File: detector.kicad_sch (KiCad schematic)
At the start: 16 parts, among them Q3 KT315, U1 74HC08, U5 LM339

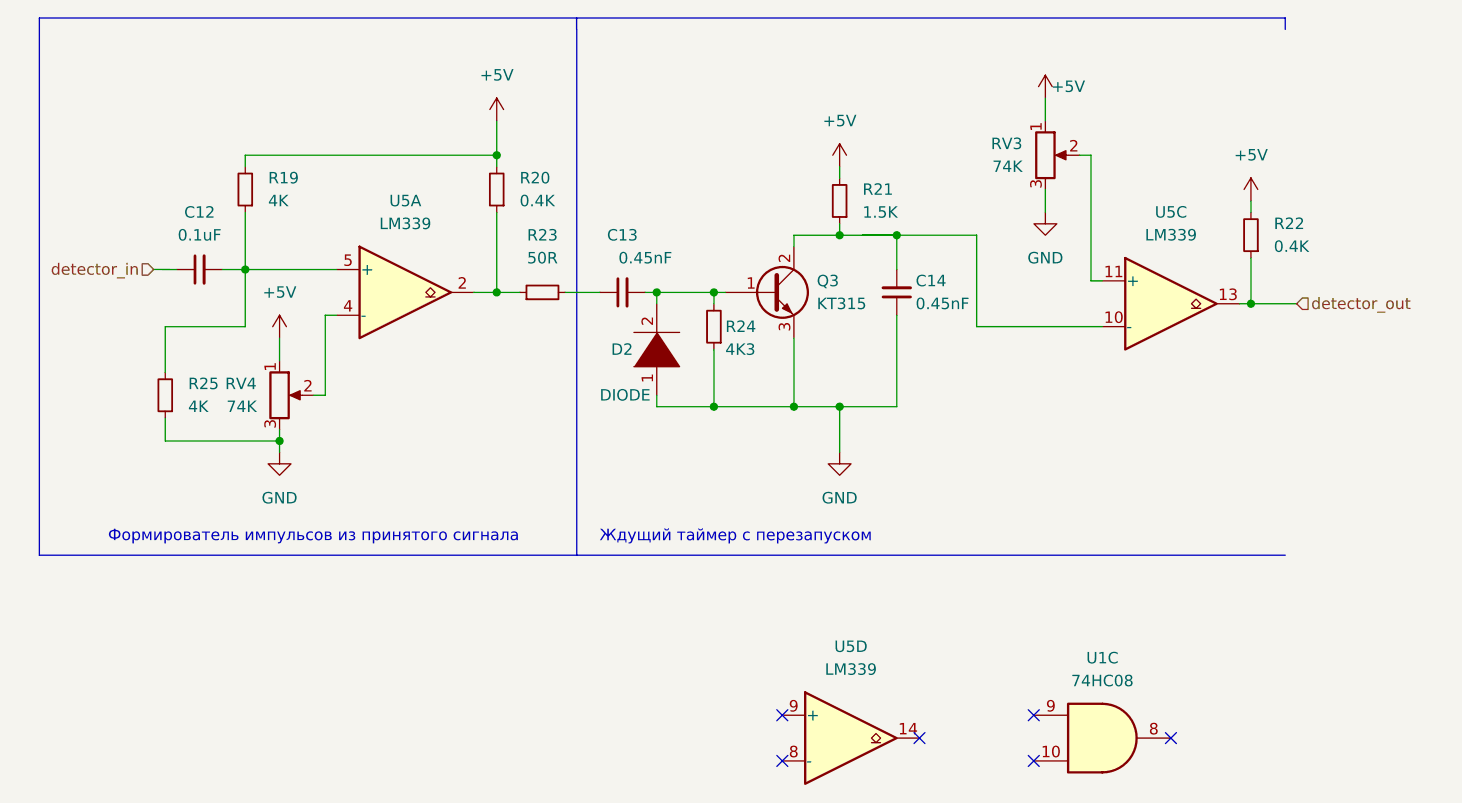
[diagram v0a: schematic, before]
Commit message: test points and some silk added
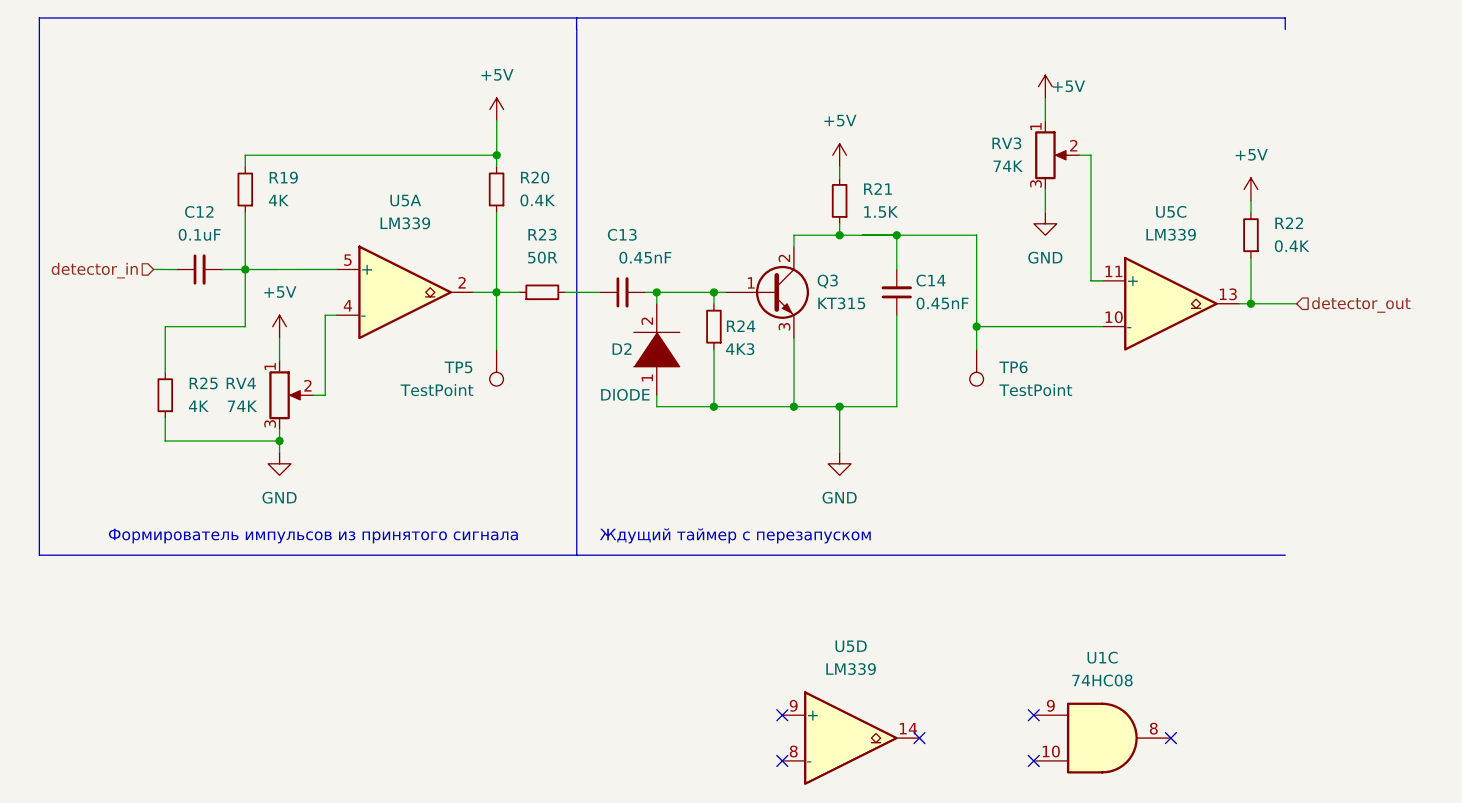
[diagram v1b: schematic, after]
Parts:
- added TP5, TP6: TestPoint, TestPoint:TestPoint_Pad_D1.0mm, symbol Connector:TestPoint
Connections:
- net at R20.1, R23.1, U5.2: now also TP5.1
- net at C14.2, Q3.2 (C), R21.1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: now also TP6.1
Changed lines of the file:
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@@
   (junction (at 146.068 104.1488) (diameter 0) (color 0 0 0 0)
   )
-  (junction (at 113.048 91.4488) (diameter 0) (color 0 0 0 0)
+  (junction (at 166.37 95.25) (diameter 0) (color 0 0 0 0)
   )
   (junction (at 196.85 92.71) (diameter 0) (color 0 0 0 0)
@@
   )
   (junction (at 137.178 104.1488) (diameter 0) (color 0 0 0 0)
+  )
+  (junction (at 113.03 91.44) (diameter 0) (color 0 0 0 0)
   )
   (junction (at 88.918 107.9588) (diameter 0) (color 0 0 0 0)
@@
   (no_connect (at 144.78 143.51))
   (no_connect (at 160.02 140.97))
+  (wire (pts (xy 113.03 91.44) (xy 113.03 97.79))
+    (stroke (width 0) (type default) (color 0 0 0 0))
+  )
   (wire (pts (xy 85.108 82.5588) (xy 85.108 88.9088))
     (stroke (width 0) (type default) (color 0 0 0 0))
@@
     (stroke (width 0) (type default) (color 0 0 0 0))
   )
-  (wire (pts (xy 113.048 91.4488) (xy 115.588 91.4488))
-    (stroke (width 0) (type default) (color 0 0 0 0))
-  )
   (wire (pts (xy 137.178 104.1488) (xy 146.068 104.1488))
     (stroke (width 0) (type default) (color 0 0 0 0))
@@
     (stroke (width 0) (type default) (color 0 0 0 0))
   )
+  (wire (pts (xy 113.03 82.55) (xy 113.03 91.44))
+    (stroke (width 0) (type default) (color 0 0 0 0))
+  )
   (wire (pts (xy 129.558 91.4488) (xy 130.828 91.4488))
     (stroke (width 0) (type default) (color 0 0 0 0))
   )
-  (wire (pts (xy 113.048 76.2088) (xy 113.048 77.4788))
+  (wire (pts (xy 113.03 91.44) (xy 115.57 91.44))
+    (stroke (width 0) (type default) (color 0 0 0 0))
+  )
+  (wire (pts (xy 113.048 76.2088) (xy 113.03 77.47))
     (stroke (width 0) (type default) (color 0 0 0 0))
   )
@@
     (stroke (width 0) (type default) (color 0 0 0 0))
   )
-  (wire (pts (xy 85.108 88.9088) (xy 95.268 88.9088))
-    (stroke (width 0) (type default) (color 0 0 0 0))
-  )
-  (wire (pts (xy 113.048 82.5588) (xy 113.048 91.4488))
-    (stroke (width 0) (type default) (color 0 0 0 0))
-  )
-  (wire (pts (xy 120.668 91.4488) (xy 124.478 91.4488))
+  (wire (pts (xy 110.49 91.44) (xy 113.03 91.44))
+    (stroke (width 0) (type default) (color 0 0 0 0))
+  )
+  (wire (pts (xy 85.108 88.9088) (xy 95.25 88.9))
+    (stroke (width 0) (type default) (color 0 0 0 0))
+  )
+  (wire (pts (xy 120.65 91.44) (xy 124.478 91.4488))
     (stroke (width 0) (type default) (color 0 0 0 0))
   )
@@
     (stroke (width 0) (type default) (color 0 0 0 0))
   )
-  (wire (pts (xy 110.508 91.4488) (xy 113.048 91.4488))
+  (wire (pts (xy 166.37 95.25) (xy 166.37 97.79))
     (stroke (width 0) (type default) (color 0 0 0 0))
   )
@@
     (stroke (width 0) (type default) (color 0 0 0 0))
   )
-  (wire (pts (xy 95.268 93.9888) (xy 93.998 93.9888))
+  (wire (pts (xy 95.25 93.98) (xy 93.998 93.9888))
     (stroke (width 0) (type default) (color 0 0 0 0))
   )
@@
     (effects (font (size 1.27 1.27)) (justify right))
   )
-  (symbol (lib_id "Device:R_Small") (at 118.128 91.4488 90) (unit 1)
-    (in_bom yes) (on_board yes) (fields_autoplaced)
-    (property "Reference" "R23" (id 0) (at 118.128 85.0988 90))
-    (property "Value" "50R" (id 1) (at 118.128 87.6388 90))
-    (property "Footprint" "Resistor_SMD:R_0603_1608Metric" (id 2) (at 118.128 91.4488 0)
-      (effects (font (size 1.27 1.27)) hide)
-    )
-    (property "Datasheet" "~" (id 3) (at 118.128 91.4488 0)
+  (symbol (lib_id "Device:R_Small") (at 118.11 91.44 90) (unit 1)
+    (in_bom yes) (on_board yes) (fields_autoplaced)
+    (property "Reference" "R23" (id 0) (at 118.11 85.09 90))
+    (property "Value" "50R" (id 1) (at 118.11 87.63 90))
+    (property "Footprint" "Resistor_SMD:R_0603_1608Metric" (id 2) (at 118.11 91.44 0)
+      (effects (font (size 1.27 1.27)) hide)
+    )
+    (property "Datasheet" "~" (id 3) (at 118.11 91.44 0)
       (effects (font (size 1.27 1.27)) hide)
     )
@@
     (pin "3")
   )
+  (symbol (lib_id "Connector:TestPoint") (at 113.03 97.79 0) (mirror x) (unit 1)
+    (in_bom yes) (on_board yes) (fields_autoplaced)
+    (property "Reference" "TP5" (id 0) (at 110.49 99.8219 0)
+      (effects (font (size 1.27 1.27)) (justify right))
+    )
+    (property "Value" "TestPoint" (id 1) (at 110.49 102.3619 0)
+      (effects (font (size 1.27 1.27)) (justify right))
+    )
+    (property "Footprint" "TestPoint:TestPoint_Pad_D1.0mm" (id 2) (at 118.11 97.79 0)
+      (effects (font (size 1.27 1.27)) hide)
+    )
+    (property "Datasheet" "~" (id 3) (at 118.11 97.79 0)
+      (effects (font (size 1.27 1.27)) hide)
+    )
+    (pin "1")
+  )
   (symbol (lib_id "Device:R_Potentiometer") (at 174.008 76.2088 0) (unit 1)
     (in_bom yes) (on_board yes) (fields_autoplaced)
@@
     (pin "1")
   )
-  (symbol (lib_id "Comparator:LM339") (at 102.888 91.4488 0) (unit 1)
-    (in_bom yes) (on_board yes) (fields_autoplaced)
-    (property "Reference" "U5" (id 0) (at 102.888 81.2888 0))
-    (property "Value" "LM339" (id 1) (at 102.888 83.8288 0))
-    (property "Footprint" "Package_SO:SO-14_3.9x8.65mm_P1.27mm" (id 2) (at 101.618 88.9088 0)
-      (effects (font (size 1.27 1.27)) hide)
-    )
-    (property "Datasheet" "https://www.st.com/resource/en/datasheet/lm139.pdf" (id 3) (at 104.158 86.3688 0)
+  (symbol (lib_id "Comparator:LM339") (at 102.87 91.44 0) (unit 1)
+    (in_bom yes) (on_board yes) (fields_autoplaced)
+    (property "Reference" "U5" (id 0) (at 102.87 81.28 0))
+    (property "Value" "LM339" (id 1) (at 102.87 83.82 0))
+    (property "Footprint" "Package_SO:SO-14_3.9x8.65mm_P1.27mm" (id 2) (at 101.6 88.9 0)
+      (effects (font (size 1.27 1.27)) hide)
+    )
+    (property "Datasheet" "https://www.st.com/resource/en/datasheet/lm139.pdf" (id 3) (at 104.14 86.36 0)
       (effects (font (size 1.27 1.27)) hide)
     )
@@
     (pin "1")
   )
+  (symbol (lib_id "Connector:TestPoint") (at 166.37 97.79 180) (unit 1)
+    (in_bom yes) (on_board yes) (fields_autoplaced)
+    (property "Reference" "TP6" (id 0) (at 168.91 99.8219 0)
+      (effects (font (size 1.27 1.27)) (justify right))
+    )
+    (property "Value" "TestPoint" (id 1) (at 168.91 102.3619 0)
+      (effects (font (size 1.27 1.27)) (justify right))
+    )
+    (property "Footprint" "TestPoint:TestPoint_Pad_D1.0mm" (id 2) (at 161.29 97.79 0)
+      (effects (font (size 1.27 1.27)) hide)
+    )
+    (property "Datasheet" "~" (id 3) (at 161.29 97.79 0)
+      (effects (font (size 1.27 1.27)) hide)
+    )
+    (pin "1")
+  )
   (symbol (lib_id "Device:R_Small") (at 76.218 102.8788 180) (unit 1)
     (in_bom yes) (on_board yes) (fields_autoplaced)
@@
     (pin "1")
   )
-  (symbol (lib_id "Device:R_Small") (at 113.048 80.0188 180) (unit 1)
-    (in_bom yes) (on_board yes) (fields_autoplaced)
-    (property "Reference" "R20" (id 0) (at 115.588 78.7487 0)
-      (effects (font (size 1.27 1.27)) (justify right))
-    )
-    (property "Value" "0.4K" (id 1) (at 115.588 81.2887 0)
-      (effects (font (size 1.27 1.27)) (justify right))
-    )
-    (property "Footprint" "Resistor_SMD:R_0603_1608Metric" (id 2) (at 113.048 80.0188 0)
-      (effects (font (size 1.27 1.27)) hide)
-    )
-    (property "Datasheet" "~" (id 3) (at 113.048 80.0188 0)
-      (effects (font (size 1.27 1.27)) hide)
-    )
+  (symbol (lib_id "Device:R_Small") (at 113.03 80.01 180) (unit 1)
+    (in_bom yes) (on_board yes) (fields_autoplaced)
+    (property "Reference" "R20" (id 0) (at 115.57 78.7399 0)
+      (effects (font (size 1.27 1.27)) (justify right))
+    )
+    (property "Value" "0.4K" (id 1) (at 115.57 81.2799 0)
+      (effects (font (size 1.27 1.27)) (justify right))
+    )
+    (property "Footprint" "Resistor_SMD:R_0603_1608Metric" (id 2) (at 113.03 80.01 0)
+      (effects (font (size 1.27 1.27)) hide)
+    )
+    (property "Datasheet" "~" (id 3) (at 113.03 80.01 0)
+      (effects (font (size 1.27 1.27)) hide)
+    )
